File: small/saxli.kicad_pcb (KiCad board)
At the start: 4 copper layers, 160.5 x 102.4 mm, 191 parts, among them IC1 PIC32MX350F256H-V_PT, IC2 SIM808, J1 78800-0001, J10 Conn_01x06_Female, J11 Conn_Coaxial, J12 Conn_Coaxial, J2 Screw_Terminal_01x02, J3 Micro_SD_Card, J4 Conn_01x05_Female, J5 Conn_02x04_Odd_Even, J6 RJ45_Amphenol_RJMG1BD3B8K1ANR, J7 Screw_Terminal_01x08, J8 Screw_Terminal_01x08, J9 Screw_Terminal_01x08, Q1 2N7002, Q2 2N7002, Q3 2N7002, U1 LM358, U10 TPS5430DDAR, U11 EL357N(C)(TA)-G, U12 EL357N(C)(TA)-G, U13 ASSR-1218, U14 ST485EBDR, U15 ASSR-1218, U16 SRV05-4, U18 ULN2003A, U2 LM7805_TO220, U20 TPS5430DDAR, U3 LD1117S33TR_SOT223, U4 ENC28J60x-SS, U5 AT25M02, U6 EL357N(C)(TA)-G, U7 EL357N(C)(TA)-G, U8 PCF8563T, U9 ISO1540, Y1 Crystal, Y2 Crystal

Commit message: ENC28j60 routed
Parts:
- U4: footprint Package_SO:SSOP-28_5.3x10.2mm_P0.65mm -> Package_SO:SOIC-28W_7.5x17.9mm_P1.27mm
- moved R21 9.18 mm to (184.3, 92.2), turned to 270 degrees
- moved R20 6.49 mm to (182.4, 92.2), turned to 270 degrees
- moved R19 5.79 mm to (187.6, 93.1)
- moved R18 5.79 mm to (187.6, 91.4)
- moved C14 4.83 mm to (193.8, 89.8)
- moved C39 4.83 mm to (193.5, 74.3)
- moved C48 4.83 mm to (193.5, 72.6)
- moved C49 4.83 mm to (193.8, 88.1)
- moved C50 4.83 mm to (193.8, 86.4)
- moved C9 4.83 mm to (193.8, 82.8)
- moved C47 4.83 mm to (193.5, 71.0)
- moved C5 4.83 mm to (193.5, 80.6)
- moved C8 4.83 mm to (193.8, 84.6)
- moved Y1 4.83 mm to (193.4, 77.6)
- moved U4 3.76 mm to (184.9, 79.8)
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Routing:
- net GND: track 1186.3 -> 1162.0 mm, vias 43 -> 46
- net /etherne/LEDA: track 51.7 -> 59.7 mm
- net VDD3: track 548.7 -> 555.9 mm, vias 17 -> 15
- net /etherne/TPIN+: track 41.3 -> 47.5 mm
- net Net-(R4-Pad2): track 2.27 -> 7.97 mm
- net ENC_RST: track 82.3 -> 86.0 mm
- net ENC_INT: track 70.0 -> 73.6 mm
- net ENC_SS: track 84.5 -> 87.9 mm
- net SCK1: track 69.0 -> 72.1 mm
- net SDI1: track 123.9 -> 126.9 mm
- net ENC_WOL: track 68.3 -> 71.2 mm
- net Net-(C14-Pad1): track 5.40 -> 8.30 mm
- net SDO1: track 115.7 -> 118.5 mm
- net /etherne/TPOUT-: track 29.6 -> 31.2 mm
- net /etherne/LEDB: track 44.8 -> 46.3 mm
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
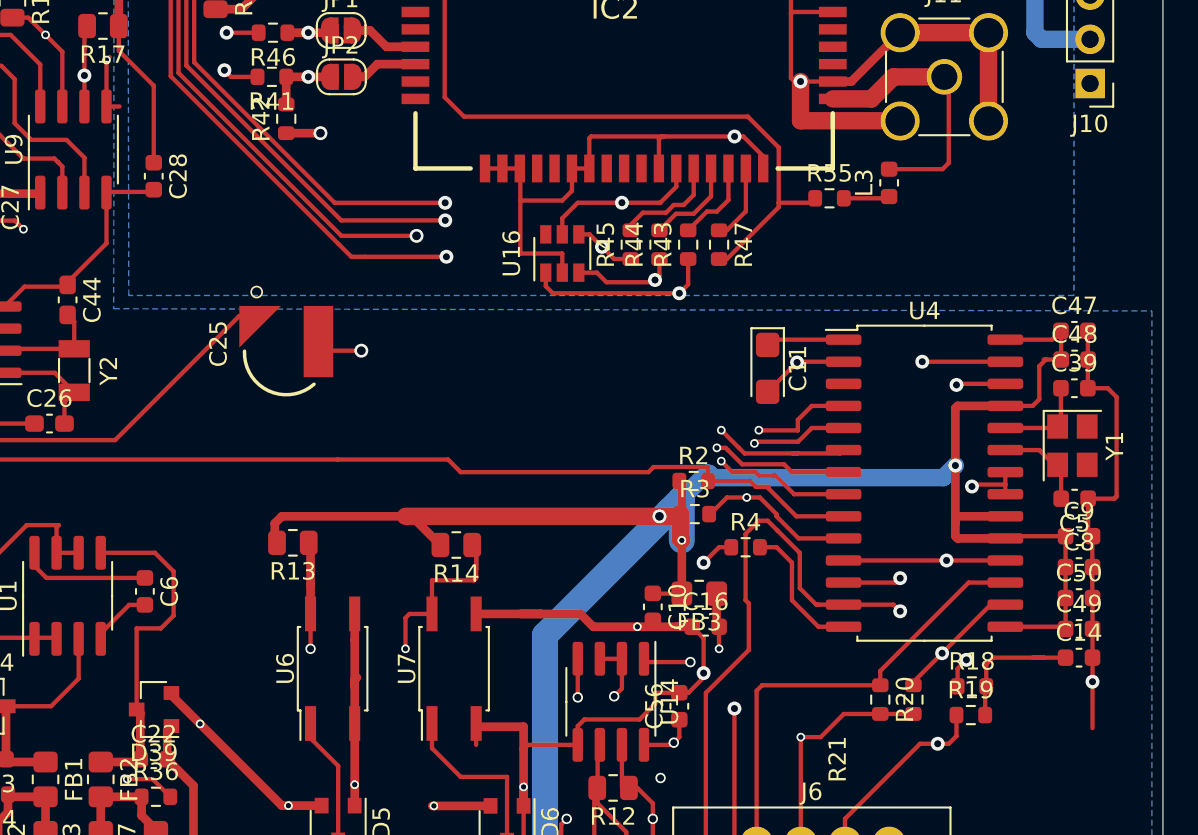
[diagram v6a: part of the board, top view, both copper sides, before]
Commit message: ENC28j60 rerouted
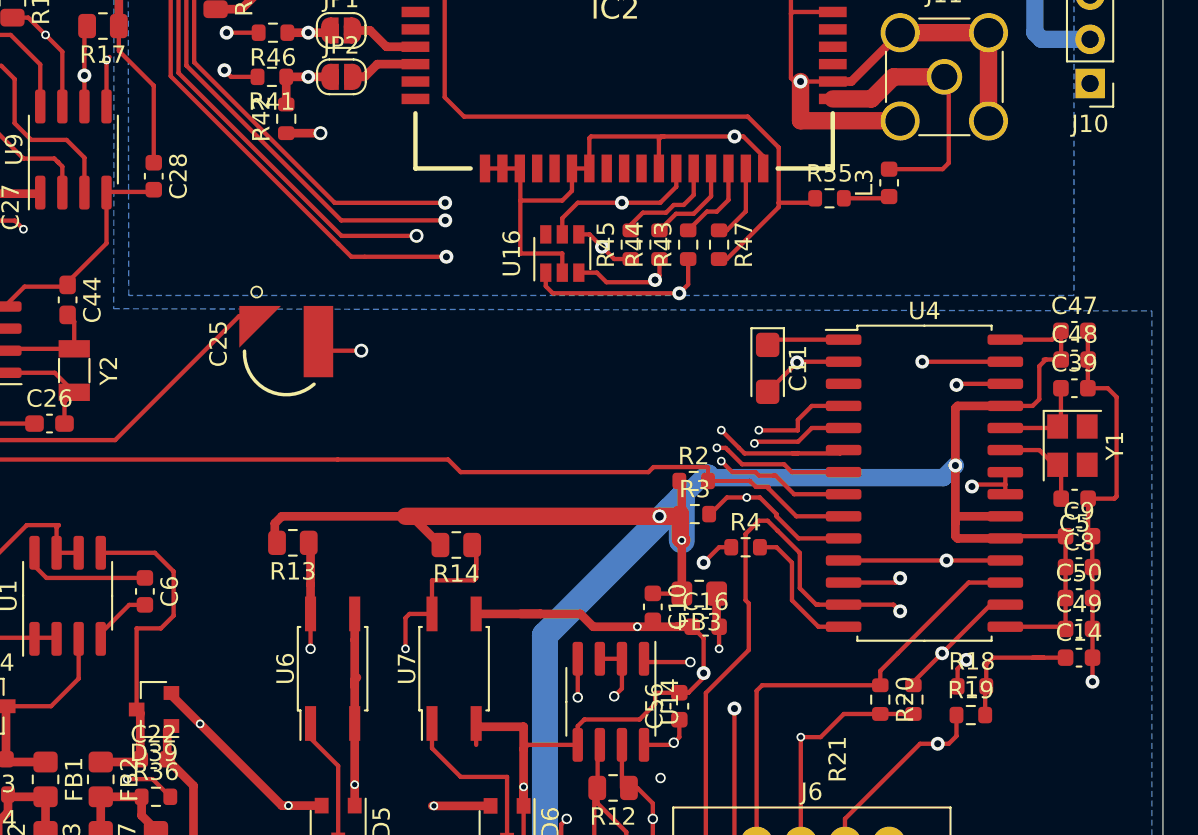
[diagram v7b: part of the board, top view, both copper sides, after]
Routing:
- net GND: track 1162.0 -> 1159.3 mm
- net /communication/GND_ISO: track 49.2 -> 48.4 mm
- net Net-(C13-Pad1): track 19.0 -> 18.4 mm
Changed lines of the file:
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@@
     (thickness 1.6)
     (drawings 7)
-    (tracks 2315)
+    (tracks 2312)
     (zones 0)
     (modules 191)
@@
   (segment (start 186.182 84.201) (end 180.262 84.201) (width 0.25) (layer F.Cu) (net 1))
   (via (at 186.182 84.201) (size 0.8) (drill 0.4) (layers F.Cu B.Cu) (net 1))
-  (segment (start 194.577 91.173) (end 194.577 93.84) (width 0.25) (layer F.Cu) (net 1))
   (via (at 194.577 91.173) (size 0.8) (drill 0.4) (layers F.Cu B.Cu) (net 1))
   (segment (start 172.212 90.678) (end 172.212 88.672) (width 0.25) (layer F.Cu) (net 1))
@@
   (segment (start 158.3055 103.378) (end 159.74 103.378) (width 0.5) (layer F.Cu) (net 19))
   (via (at 158.3055 103.378) (size 0.5) (drill 0.3) (layers F.Cu B.Cu) (net 19))
-  (segment (start 158.3055 103.378) (end 158.3055 102.8065) (width 0.25) (layer In1.Cu) (net 19))
   (segment (start 160.909 96.647) (end 158.242 96.647) (width 0.25) (layer F.Cu) (net 19))
   (segment (start 160.909 96.647) (end 160.909 100.314) (width 0.25) (layer F.Cu) (net 19))
@@
   (segment (start 93.599 65.659) (end 82.55 65.659) (width 0.25) (layer F.Cu) (net 33))
   (segment (start 102.1725 67.183) (end 95.123 67.183) (width 0.25) (layer F.Cu) (net 33))
-  (segment (start 137.872 58.093) (end 138.624 58.093) (width 0.25) (layer F.Cu) (net 34))
   (segment (start 137.872 58.093) (end 137.872 55.422) (width 0.25) (layer F.Cu) (net 34))
   (segment (start 137.872 55.422) (end 137.872 55.422) (width 0.25) (layer F.Cu) (net 34))

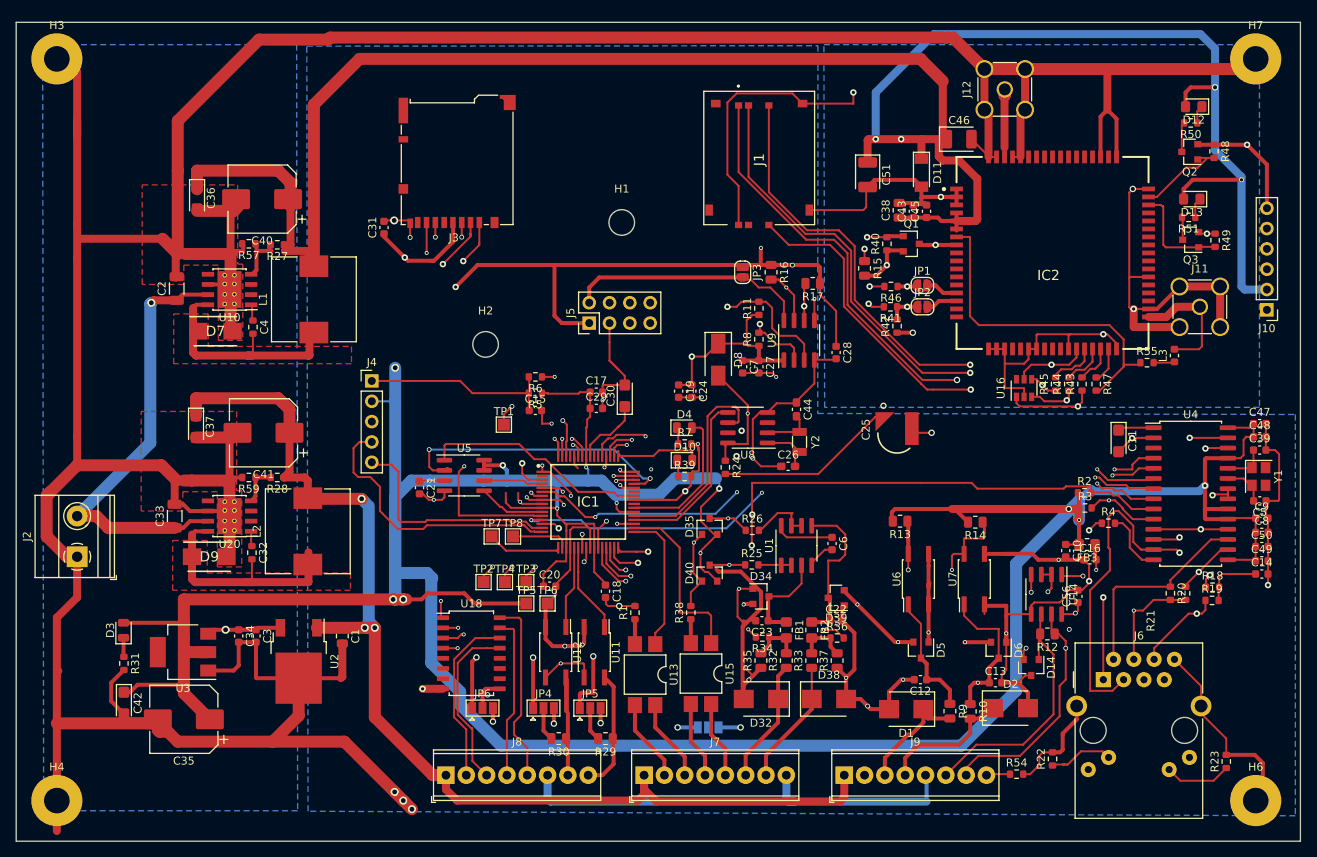
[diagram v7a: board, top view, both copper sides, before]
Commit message: SPI change:
ENC28j60 on one spi
SDCARD and EEPROM on the other.
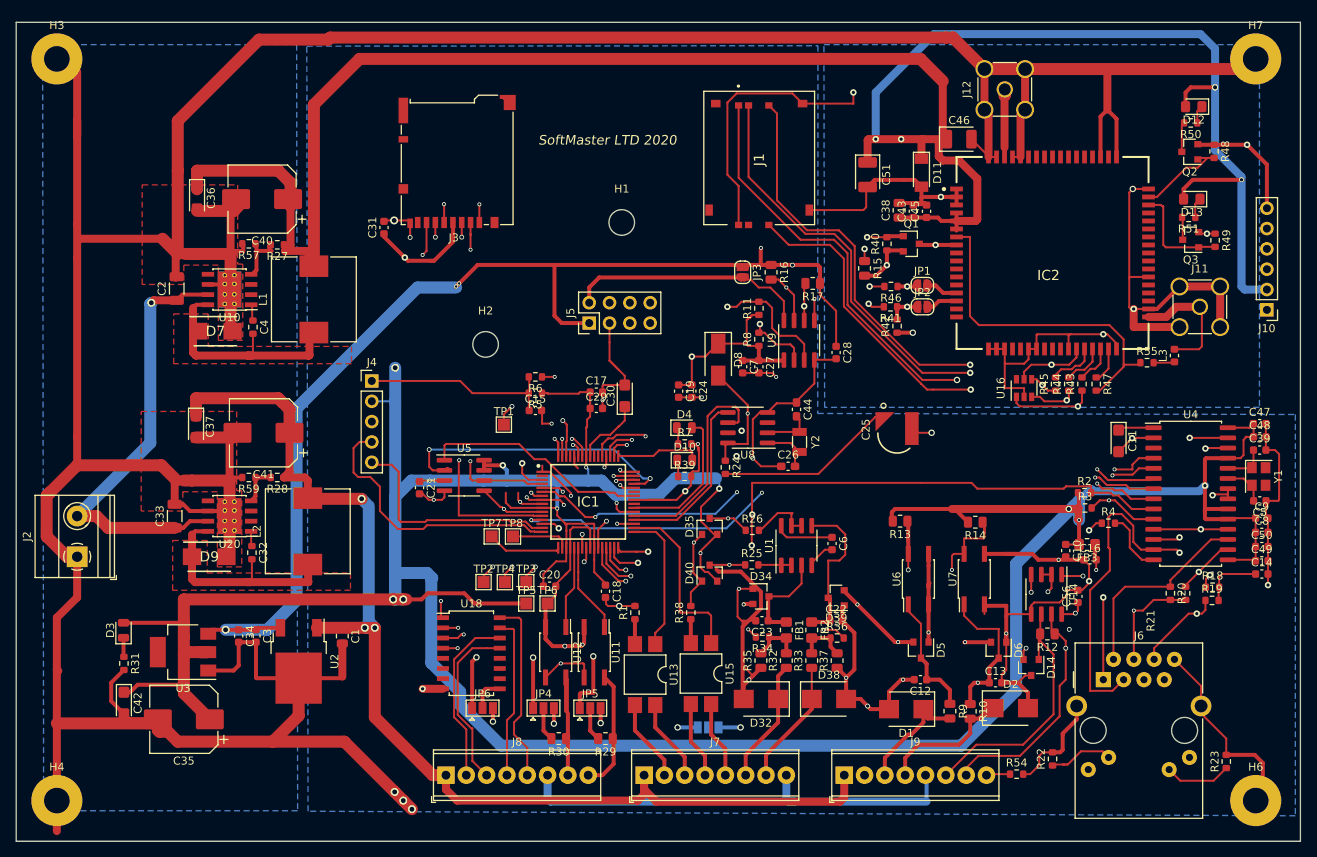
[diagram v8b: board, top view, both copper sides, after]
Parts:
- R4: value 2k 1% -> 2.32k 1%
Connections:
- J3 pad 1: SDO1 -> SDO2
- J3 pad 5: CLK1 -> SCK2
- J3 pad 7: SDI1 -> SDI2
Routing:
- net SDI1: track 126.9 -> 78.7 mm, vias 4 -> 2
- net SDO2: track 8.38 -> 52.9 mm, vias 0 -> 2
- net SCK2: track 7.45 -> 47.5 mm, vias 0 -> 2
- net SDO1: track 118.5 -> 81.8 mm, vias 4 -> 2
- net SDI2: track 36.4 -> 65.4 mm, vias 2 -> 3
- net VDD5: track 332.5 -> 328.7 mm, vias 9 -> 10
- net SD_CS: track 40.1 -> 36.4 mm
- net U2RX: track 22.8 -> 19.5 mm
- net U2TX: track 21.8 -> 20.0 mm
- net /etherne/LEDA: track 59.7 -> 61.5 mm
- net Net-(C32-Pad2): track 29.6 -> 28.1 mm
- net /etherne/TPOUT+: track 26.1 -> 25.5 mm
- net 12V: track 218.0 -> 218.6 mm
